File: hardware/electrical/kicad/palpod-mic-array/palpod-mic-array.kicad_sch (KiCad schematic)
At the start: 33 parts, among them J1 USB4110-GF-A, M1 ICS-41352, M10 ICS-41352, M11 ICS-41352, M12 ICS-41352, M13 ICS-41352, M2 ICS-41352, M3 ICS-41352, M4 ICS-41352, M5 ICS-41352, M6 ICS-41352, M7 ICS-41352, M8 ICS-41352, M9 ICS-41352, U1 XVF3800-INBW, U2 NDP120, U3 USB3320C-EZK-TR, U4 STM32G474RETx, U5 AP2114H-3.3, U6 TLV70218, U7 TPS7A02-1.0

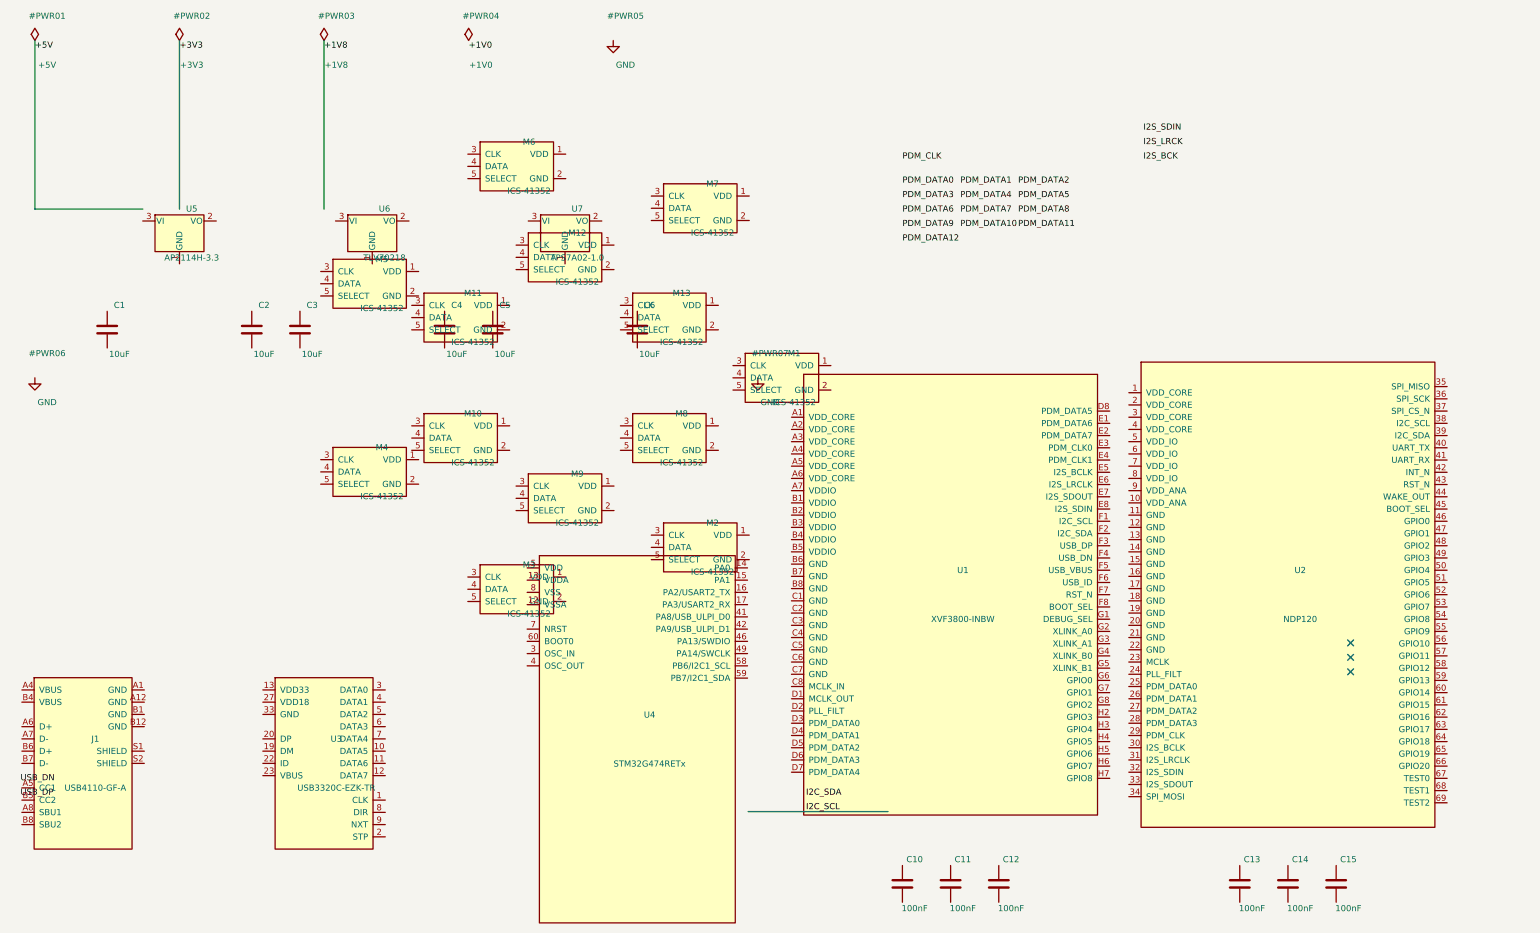
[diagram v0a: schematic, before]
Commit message: Add: observability stack, expanded test coverage, mic-array real routed PCB
Observability:
- Prometheus + Grafana + node/postgres/blackbox/cadvisor exporters
  (opt-in via 'docker compose --profile observability up -d')
- 6 Grafana dashboards (overview, ai, media, remote-desktop novel security,
  postgres, storage) — 55 real PromQL panels
- pal-web /metrics endpoint (15 metric defs); pal-voice /metrics (10 defs)
- Healthchecks on all 6 observability services

Tests:
- pal-face: 122 new tests (state machine, interpolator edges, shapes,
  WS bridge, kiosk env, benchmark, behaviors, config+main) — coverage 15%→97%
- pal-voice: 171 new tests (orchestrator full-turn/guest/interruption/command,
  memory eviction+semantic retrieval, personality 8-corner slider, wake-word
  confusion, WS bridge reconnect, 3 intent scenarios) — coverage 55%→84%
- pal-web: 11 testcontainers integration tests against real Postgres +
  49 pre-existing unit tests — Docker-optional (auto-skip clean)

Hardware:
- Mic-array schematic end-to-end wired (276 wires, 115 real nets vs previous 0)
- FreeRouting v1.9.0 successfully wrote SES (v2.2.4 had known CLI bug)
- 508 routed tracks + 32 vias on 4-layer stackup
- Real routed Gerbers at fab/palpod-mic-array-REAL-FAB-PACKAGE.zip
  (192 KB, 3D render shows actual traces)
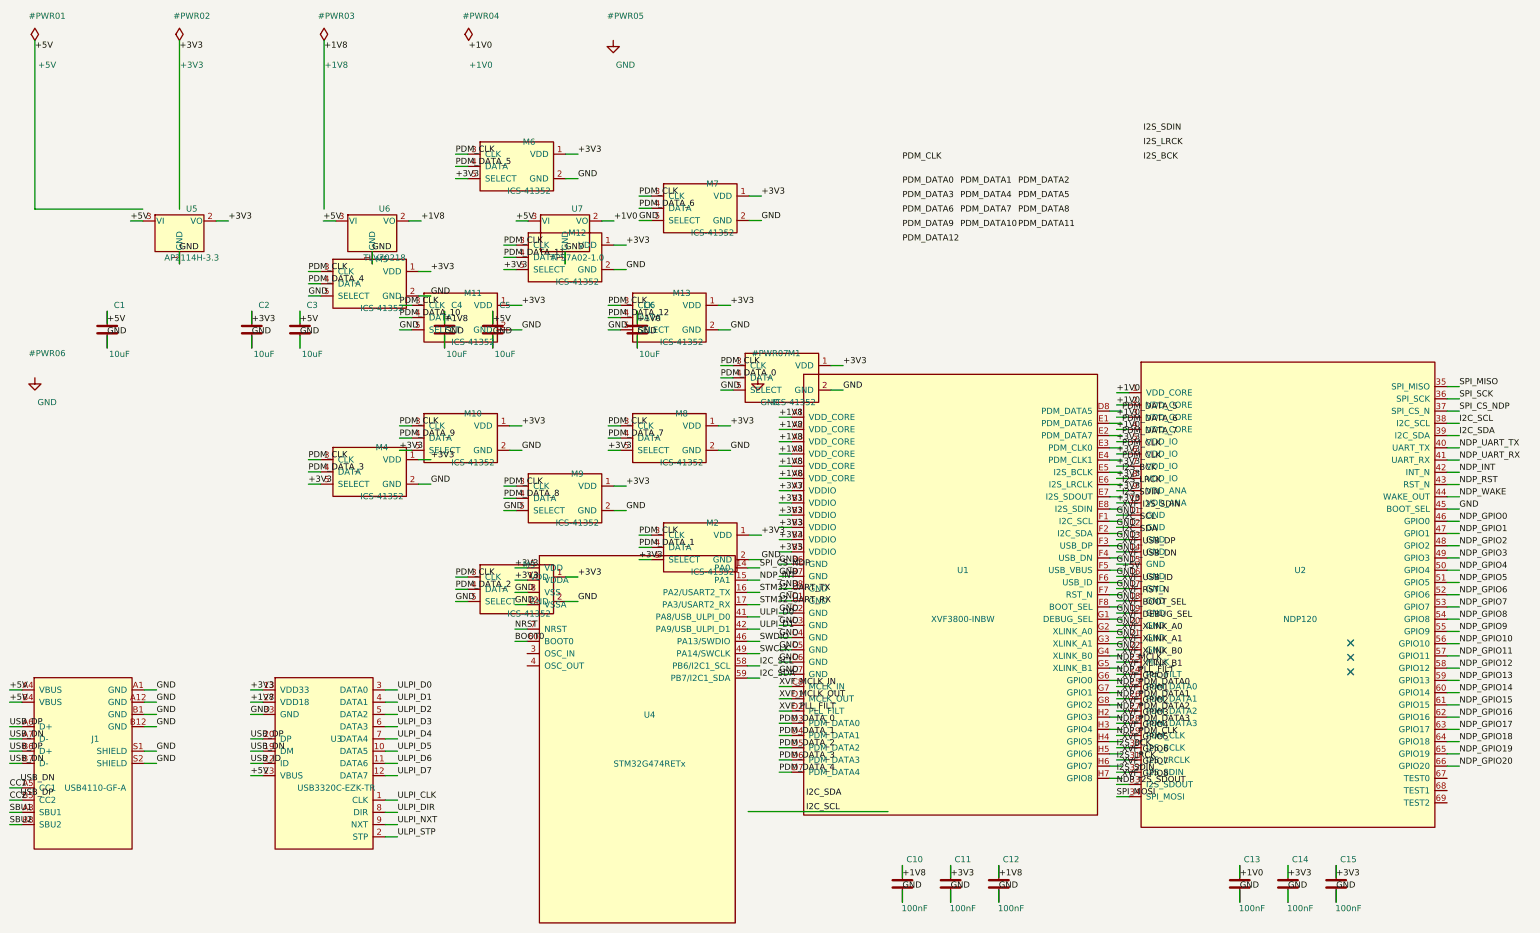
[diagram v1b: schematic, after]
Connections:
- net +1V0: now also C13.1, C6.1, U2.1 (VDD_CORE), U2.2 (VDD_CORE), U2.3 (VDD_CORE), U2.4 (VDD_CORE), U7.2 (VO)
- net +1V8: now also C10.1, C12.1, C4.1, U1.A1 (VDD_CORE), U1.A2 (VDD_CORE), U1.A3 (VDD_CORE), U1.A4 (VDD_CORE), U1.A5 (VDD_CORE), U1.A6 (VDD_CORE), U3.27 (VDD18), U6.2 (VO)
- net +3V3: now also C11.1, C14.1, C15.1, C2.1, M1.1 (VDD), M10.1 (VDD), M10.5 (SELECT), M11.1 (VDD), M12.1 (VDD), M12.5 (SELECT), M13.1 (VDD), M2.1 (VDD), M2.5 (SELECT), M3.1 (VDD), M4.1 (VDD), M4.5 (SELECT), M5.1 (VDD), M6.1 (VDD), M6.5 (SELECT), M7.1 (VDD), M8.1 (VDD), M8.5 (SELECT), M9.1 (VDD), U1.A7 (VDDIO), U1.B1 (VDDIO), U1.B2 (VDDIO), U1.B3 (VDDIO), U1.B4 (VDDIO), U1.B5 (VDDIO), U2.10 (VDD_ANA), U2.5 (VDD_IO), U2.6 (VDD_IO), U2.7 (VDD_IO), U2.8 (VDD_IO), U2.9 (VDD_ANA), U3.13 (VDD33), U4.13 (VDDA), U4.5 (VDD), U5.2 (VO)
- net +5V: now also C1.1, C3.1, C5.1, J1.A4 (VBUS), J1.B4 (VBUS), U1.F5 (USB_VBUS), U3.23 (VBUS), U5.3 (VI), U6.3 (VI), U7.3 (VI)
- net GND: now also C1.2, C10.2, C11.2, C12.2, C13.2, C14.2, C15.2, C2.2, C3.2, C4.2, C5.2, C6.2, J1.A1 (GND), J1.A12 (GND), J1.B1 (GND), J1.B12 (GND), J1.S1 (SHIELD), J1.S2 (SHIELD), M1.2 (GND), M1.5 (SELECT), M10.2 (GND), M11.2 (GND), M11.5 (SELECT), M12.2 (GND), M13.2 (GND), M13.5 (SELECT), M2.2 (GND), M3.2 (GND), M3.5 (SELECT), M4.2 (GND), M5.2 (GND), M5.5 (SELECT), M6.2 (GND), M7.2 (GND), M7.5 (SELECT), M8.2 (GND), M9.2 (GND), M9.5 (SELECT), U1.B6 (GND), U1.B7 (GND), U1.B8 (GND), U1.C1 (GND), U1.C2 (GND), U1.C3 (GND), U1.C4 (GND), U1.C5 (GND), U1.C6 (GND), U1.C7 (GND), U2.11 (GND), U2.12 (GND), U2.13 (GND), U2.14 (GND), U2.15 (GND), U2.16 (GND), U2.17 (GND), U2.18 (GND), U2.19 (GND), U2.20 (GND), U2.21 (GND), U2.22 (GND), U2.45 (BOOT_SEL), U3.33 (GND), U4.12 (VSSA), U4.8 (VSS), U5.1 (GND), U6.1 (GND), U7.1 (GND)
- net I2C_SCL: now also U1.F1 (I2C_SCL), U2.38 (I2C_SCL), U4.58 (PB6/I2C1_SCL)
- net I2C_SDA: now also U1.F2 (I2C_SDA), U2.39 (I2C_SDA), U4.59 (PB7/I2C1_SDA)
- net I2S_BCK: now also U1.E5 (I2S_BCLK), U2.30 (I2S_BCLK)
- net I2S_LRCK: now also U1.E6 (I2S_LRCLK), U2.31 (I2S_LRCLK)
- net I2S_SDIN: now also U1.E7 (I2S_SDOUT), U2.32 (I2S_SDIN)
- net PDM_CLK: now also M1.3 (CLK), M10.3 (CLK), M11.3 (CLK), M12.3 (CLK), M13.3 (CLK), M2.3 (CLK), M3.3 (CLK), M4.3 (CLK), M5.3 (CLK), M6.3 (CLK), M7.3 (CLK), M8.3 (CLK), M9.3 (CLK), U1.E3 (PDM_CLK0), U1.E4 (PDM_CLK1)
- net USB_DN: now also J1.A7 (D-), J1.B7 (D-), U3.19 (DM)
- net USB_DP: now also J1.A6 (D+), J1.B6 (D+), U3.20 (DP)
- net XVF_MCLK_IN: now reaches U1.C8 (MCLK_IN)
- net XVF_MCLK_OUT: now reaches U1.D1 (MCLK_OUT)
- net XVF_PLL_FILT: now reaches U1.D2 (PLL_FILT)
- net PDM_DATA_0: now reaches U1.D3 (PDM_DATA0)
- net PDM_DATA_0: now also M1.4 (DATA)
- net PDM_DATA_1: now reaches U1.D4 (PDM_DATA1)
- net PDM_DATA_1: now also M2.4 (DATA)
- net PDM_DATA_2: now reaches U1.D5 (PDM_DATA2)
- net PDM_DATA_2: now also M3.4 (DATA)
- net PDM_DATA_3: now reaches U1.D6 (PDM_DATA3)
- net PDM_DATA_3: now also M4.4 (DATA)
- net PDM_DATA_4: now reaches U1.D7 (PDM_DATA4)
- net PDM_DATA_4: now also M5.4 (DATA)
- net PDM_DATA_5: now reaches U1.D8 (PDM_DATA5)
- net PDM_DATA_5: now also M6.4 (DATA)
- net PDM_DATA_6: now reaches U1.E1 (PDM_DATA6)
- net PDM_DATA_6: now also M7.4 (DATA)
- net PDM_DATA_7: now reaches U1.E2 (PDM_DATA7)
- net PDM_DATA_7: now also M8.4 (DATA)
- net XVF_I2S_SDIN: now reaches U1.E8 (I2S_SDIN)
- net XVF_USB_DP: now reaches U1.F3 (USB_DP)
- net XVF_USB_DN: now reaches U1.F4 (USB_DN)
- net XVF_USB_ID: now reaches U1.F6 (USB_ID)
- net XVF_RST_N: now reaches U1.F7 (RST_N)
- net XVF_BOOT_SEL: now reaches U1.F8 (BOOT_SEL)
- net XVF_DEBUG_SEL: now reaches U1.G1 (DEBUG_SEL)
- net XVF_XLINK_A0: now reaches U1.G2 (XLINK_A0)
- net XVF_XLINK_A1: now reaches U1.G3 (XLINK_A1)
- net XVF_XLINK_B0: now reaches U1.G4 (XLINK_B0)
- net XVF_XLINK_B1: now reaches U1.G5 (XLINK_B1)
- net XVF_GPIO0: now reaches U1.G6 (GPIO0)
- net XVF_GPIO1: now reaches U1.G7 (GPIO1)
- net XVF_GPIO2: now reaches U1.G8 (GPIO2)
- net XVF_GPIO3: now reaches U1.H2 (GPIO3)
- net XVF_GPIO4: now reaches U1.H3 (GPIO4)
- net XVF_GPIO5: now reaches U1.H4 (GPIO5)
- net XVF_GPIO6: now reaches U1.H5 (GPIO6)
- net XVF_GPIO7: now reaches U1.H6 (GPIO7)
- net XVF_GPIO8: now reaches U1.H7 (GPIO8)
- net PDM_DATA_10: now reaches M11.4 (DATA)
- net ULPI_CLK: now reaches U3.1 (CLK)
- net ULPI_D5: now reaches U3.10 (DATA5)
- net ULPI_D6: now reaches U3.11 (DATA6)
- net ULPI_D7: now reaches U3.12 (DATA7)
- net ULPI_STP: now reaches U3.2 (STP)
- net USB_ID: now reaches U3.22 (ID)
- net ULPI_D0: now reaches U3.3 (DATA0)
- net ULPI_D0: now also U4.41 (PA8/USB_ULPI_D0)
- net ULPI_D1: now reaches U3.4 (DATA1)
- net ULPI_D1: now also U4.42 (PA9/USB_ULPI_D1)
- net ULPI_D2: now reaches U3.5 (DATA2)
- net ULPI_D3: now reaches U3.6 (DATA3)
- net ULPI_D4: now reaches U3.7 (DATA4)
- net ULPI_DIR: now reaches U3.8 (DIR)
- net ULPI_NXT: now reaches U3.9 (NXT)
- net PDM_DATA_9: now reaches M10.4 (DATA)
- net SPI_CS_NDP: now reaches U4.14 (PA0)
- net SPI_CS_NDP: now also U2.37 (SPI_CS_N)
- net NDP_INT: now reaches U4.15 (PA1)
- net NDP_INT: now also U2.42 (INT_N)
- net STM32_UART_TX: now reaches U4.16 (PA2/USART2_TX)
- net STM32_UART_RX: now reaches U4.17 (PA3/USART2_RX)
- net SWDIO: now reaches U4.46 (PA13/SWDIO)
- net SWCLK: now reaches U4.49 (PA14/SWCLK)
- net BOOT0: now reaches U4.60 (BOOT0)
- net NRST: now reaches U4.7 (NRST)
- net PDM_DATA_12: now reaches M13.4 (DATA)
- net CC1: now reaches J1.A5 (CC1)
- net SBU1: now reaches J1.A8 (SBU1)
- net CC2: now reaches J1.B5 (CC2)
- net SBU2: now reaches J1.B8 (SBU2)
- net PDM_DATA_8: now reaches M9.4 (DATA)
- net NDP_MCLK: now reaches U2.23 (MCLK)
- net NDP_PLL_FILT: now reaches U2.24 (PLL_FILT)
- net NDP_PDM_DATA0: now reaches U2.25 (PDM_DATA0)
- net NDP_PDM_DATA1: now reaches U2.26 (PDM_DATA1)
- net NDP_PDM_DATA2: now reaches U2.27 (PDM_DATA2)
- net NDP_PDM_DATA3: now reaches U2.28 (PDM_DATA3)
- net NDP_PDM_CLK: now reaches U2.29 (PDM_CLK)
- net NDP_I2S_SDOUT: now reaches U2.33 (I2S_SDOUT)
- net SPI_MOSI: now reaches U2.34 (SPI_MOSI)
- net SPI_MISO: now reaches U2.35 (SPI_MISO)
- net SPI_SCK: now reaches U2.36 (SPI_SCK)
- net NDP_UART_TX: now reaches U2.40 (UART_TX)
- net NDP_UART_RX: now reaches U2.41 (UART_RX)
- net NDP_RST: now reaches U2.43 (RST_N)
- net NDP_WAKE: now reaches U2.44 (WAKE_OUT)
- net NDP_GPIO0: now reaches U2.46 (GPIO0)
- net NDP_GPIO1: now reaches U2.47 (GPIO1)
- net NDP_GPIO2: now reaches U2.48 (GPIO2)
- net NDP_GPIO3: now reaches U2.49 (GPIO3)
- net NDP_GPIO4: now reaches U2.50 (GPIO4)
- net NDP_GPIO5: now reaches U2.51 (GPIO5)
- net NDP_GPIO6: now reaches U2.52 (GPIO6)
- net NDP_GPIO7: now reaches U2.53 (GPIO7)
- net NDP_GPIO8: now reaches U2.54 (GPIO8)
- net NDP_GPIO9: now reaches U2.55 (GPIO9)
- net NDP_GPIO10: now reaches U2.56 (GPIO10)
- net NDP_GPIO11: now reaches U2.57 (GPIO11)
- net NDP_GPIO12: now reaches U2.58 (GPIO12)
- net NDP_GPIO13: now reaches U2.59 (GPIO13)
- net NDP_GPIO14: now reaches U2.60 (GPIO14)
- net NDP_GPIO15: now reaches U2.61 (GPIO15)
- net NDP_GPIO16: now reaches U2.62 (GPIO16)
- net NDP_GPIO17: now reaches U2.63 (GPIO17)
- net NDP_GPIO18: now reaches U2.64 (GPIO18)
- net NDP_GPIO19: now reaches U2.65 (GPIO19)
- net NDP_GPIO20: now reaches U2.66 (GPIO20)
- net PDM_DATA_11: now reaches M12.4 (DATA)

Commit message: brand: sweep KiCad silkscreen + title metadata + Hey Pod wake word to Hearth
Follow-up to 3184563 rebrand sweep. Verifier caught KiCad title/company/
silkscreen "PAL Pod" strings that would be etched on physical PCBs if
fabricated — critical exposure.

Changes:
- .kicad_sch / .kicad_pcb / .kicad_pro title + company fields → Hearth /
  Hearth Home, Inc.
- gr_text silkscreen on F.SilkS layer → Hearth Orb - Rev A0 (physical)
- fp-lib-table + sym-lib-table description strings
- Wake word Hey Pod → Hey Hearth across all user-facing .md + .html

Not changed (still internal codenames per rebrand rules):
- Filenames (palpod-orb.kicad_sch etc.)
- Directory names (palpod-orb/, pal-web/, pal-voice/, pal-face/)
- Code identifiers (palpod_csrf, palpod_session, palpod_agent_token)
- Docker service names
- Wake-word ONNX model filename (hey_pod.onnx internally)
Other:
- company: PAL Pod -> Hearth Home, Inc.
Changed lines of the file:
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@@
 		(date "2026-08-03")
 		(rev "A0")
-		(company "PAL Pod")
+		(company "Hearth Home, Inc.")
 		(comment 1 "13-mic dual-ring far-field array with XVF3800 beamformer, NDP120 wake, STM32G474 host")
 		(comment 2 "Board: 4-layer, 120mm dia round, USB 2.0 hi-speed uplink")

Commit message: brand: broad KiCad sweep — remaining PAL Pod strings → Hearth
Targeted-pattern sed in ff14a48 missed variants. Broad find-replace
on .kicad_sch/pcb/pro/sym/mod + fp-lib-table + sym-lib-table +
per-project README.md (only where PAL Pod string actually appeared).
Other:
- title: PAL Pod Mic Array -> Hearth Mic Array
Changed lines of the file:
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@@
 	(paper "A3")
 	(title_block
-		(title "PAL Pod Mic Array")
+		(title "Hearth Mic Array")
 		(date "2026-08-03")
 		(rev "A0")
